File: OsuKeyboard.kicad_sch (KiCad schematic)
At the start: 31 parts, among them J1 USB_B_Micro, J2 Conn_01x04_Female, SW1 SW_Push, SW2 SW_Push, SW3 RotaryEncoder_Switch, U1 STM32F401RBTx, U2 AMS1117-3.3, Y1 16MHz

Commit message: Changed MCU and layout
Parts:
- removed C7: 100n, Capacitor_SMD:C_0402_1005Metric_Pad0.74x0.62mm_HandSolder, symbol Device:C
- removed U1: STM32F401RBTx, Package_QFP:LQFP-64_10x10mm_P0.5mm, symbol MCU_ST_STM32F4:STM32F401RBTx
- added U1: STM32F103C6Tx, Package_QFP:LQFP-48_7x7mm_P0.5mm, symbol MCU_ST_STM32F1:STM32F103C6Tx
- C10, C11: footprint Capacitor_SMD:C_0805_2012Metric_Pad1.18x1.45mm_HandSolder -> Capacitor_SMD:C_0402_1005Metric_Pad0.74x0.62mm_HandSolder
- C5, C8, C9: footprint Capacitor_SMD:C_0201_0603Metric_Pad0.64x0.40mm_HandSolder -> Capacitor_SMD:C_0402_1005Metric_Pad0.74x0.62mm_HandSolder
- R1: footprint Resistor_SMD:R_0805_2012Metric -> Resistor_SMD:R_0402_1005Metric_Pad0.72x0.64mm_HandSolder
- R2, R3, R4: footprint Resistor_SMD:R_0201_0603Metric_Pad0.64x0.40mm_HandSolder -> Resistor_SMD:R_0402_1005Metric_Pad0.72x0.64mm_HandSolder
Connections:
- net +3.3V: now also U1.1 (VBAT), U1.24 (VDD), U1.36 (VDD), U1.48 (VDD), U1.9 (VDDA)
- net GND: now also U1.23 (VSS), U1.35 (VSS), U1.47 (VSS), U1.8 (VSSA)
- net boot0: now also U1.44 (BOOT0)
- net nrst: now also U1.7 (NRST)
- net osc_in: now also U1.5 (PD0)
- net osc_out: now also U1.6 (PD1)
- net rgb1b: now also U1.18 (PB0)
- net rgb1g: now also U1.19 (PB1)
- net rgb1r: now also U1.20 (PB2)
- net rgb2b: now also U1.17 (PA7)
- net rgb2g: now also U1.16 (PA6)
- net rgb2r: now also U1.15 (PA5)
- net sw1: now also U1.22 (PB11)
- net sw2: now also U1.21 (PB10)
- net swclk: now also U1.37 (PA14)
- net swdio: now also U1.34 (PA13)
- net usb+: now also U1.33 (PA12)
- net usb-: now also U1.32 (PA11)
- net Rot_Encoder_A renamed rot_encoder_a
- net rot_encoder_a: now also U1.41 (PB5)
- net Rot_Encoder_B renamed rot_encoder_b
- net rot_encoder_b: now also U1.40 (PB4)
- net Rot_Encoder_SW renamed rot_encoder_sw
- net rot_encoder_sw: now also U1.39 (PB3)
- no-connect marks 34 -> 21
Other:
- moved on the sheet: C10, C11, C8, C9, D3, H1, H2, H3, H4, J1, J2, R4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

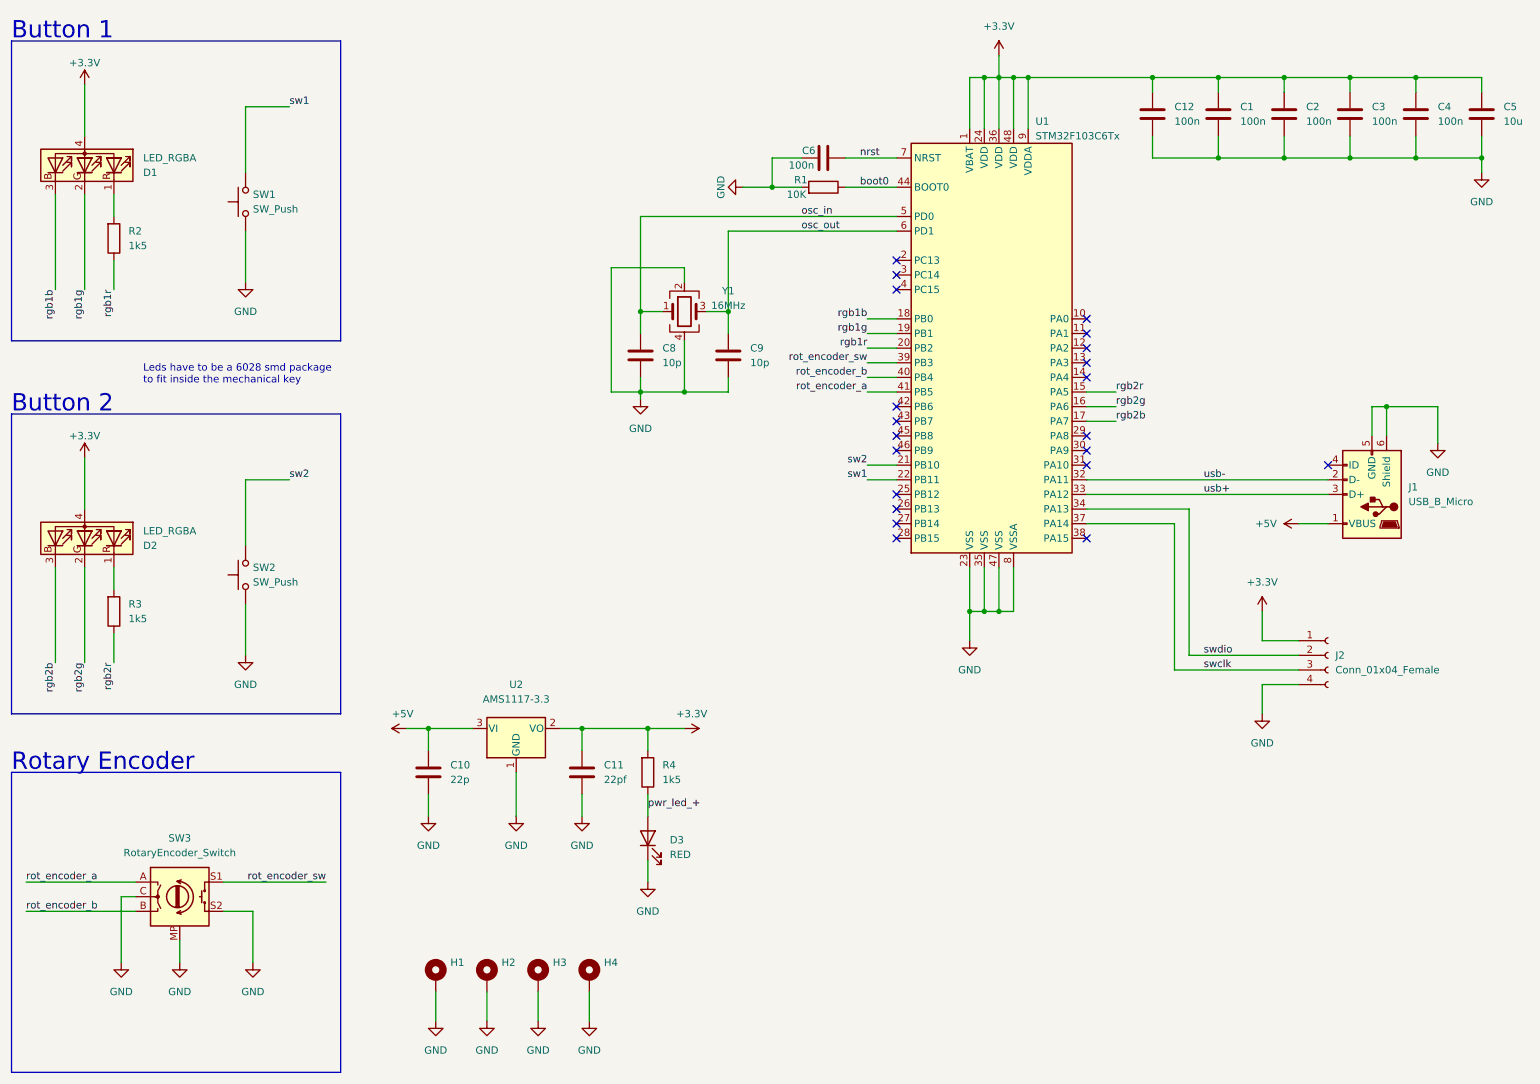
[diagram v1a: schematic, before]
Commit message: simplified and made pcb smaller
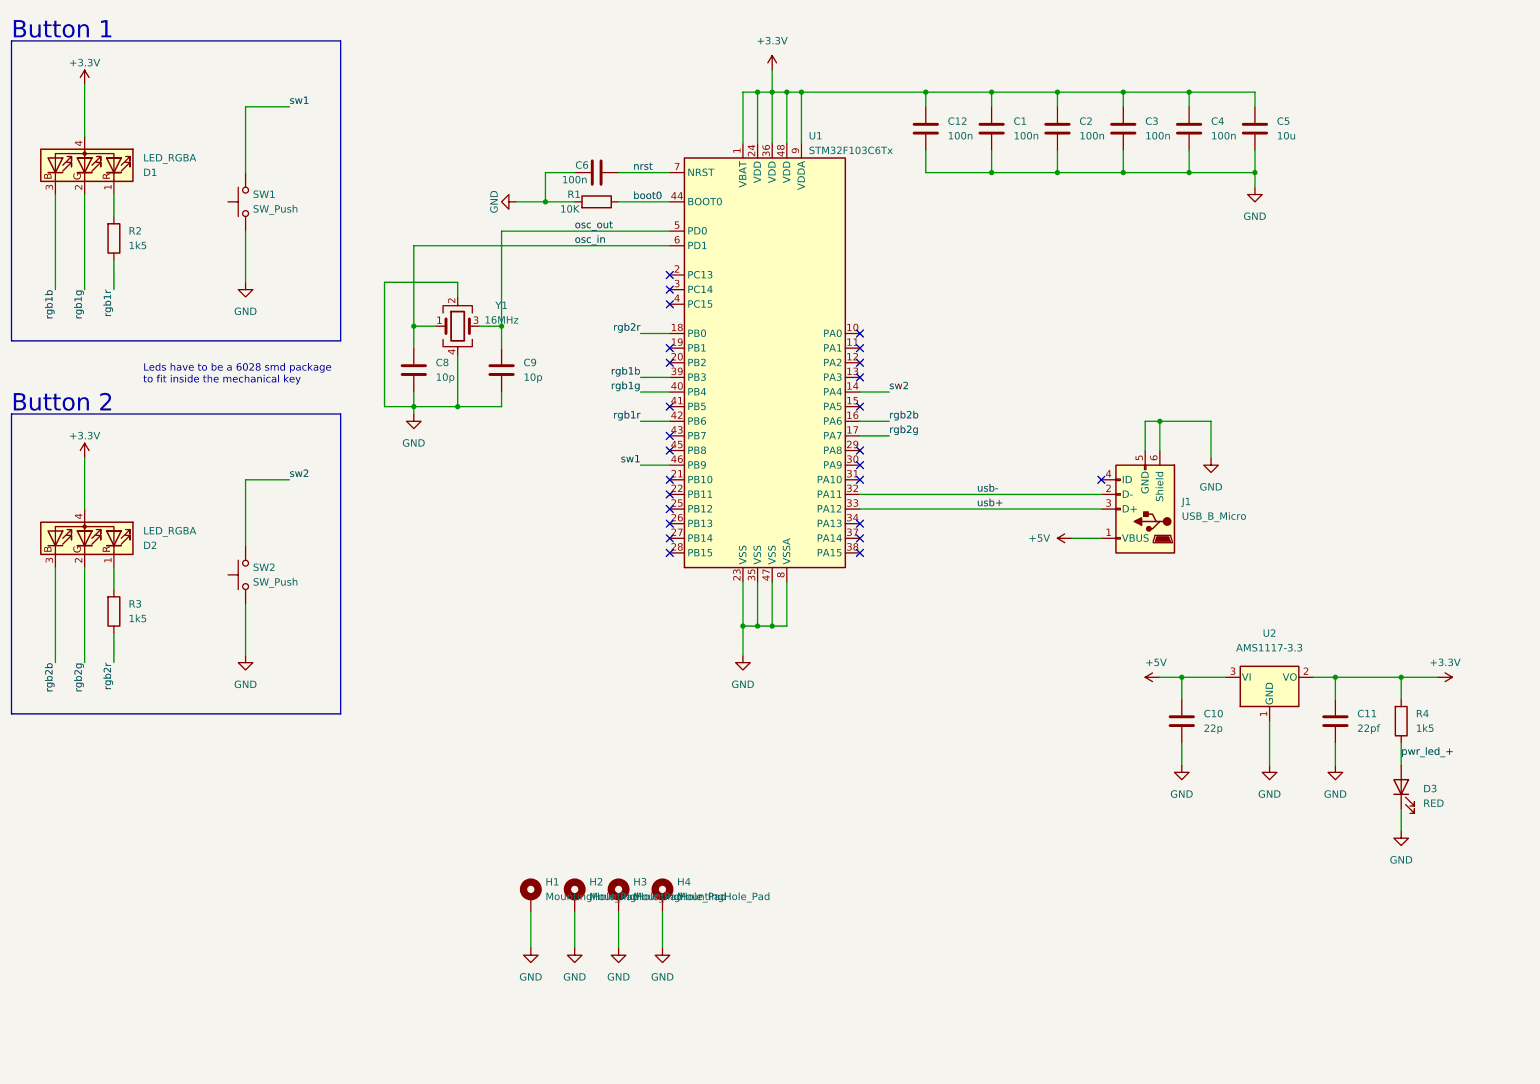
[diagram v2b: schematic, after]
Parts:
- removed J2: Conn_01x04_Female, Connector_PinHeader_2.54mm:PinHeader_1x04_P2.54mm_Vertical, symbol Connector:Conn_01x04_Female
- removed SW3: RotaryEncoder_Switch, Rotary_Encoder:RotaryEncoder_Alps_EC12E-Switch_Vertical_H20mm_CircularMountingHoles, symbol Device:RotaryEncoder_Switch
- H1, H2, H3, H4: footprint MountingHole:MountingHole_2.2mm_M2_Pad_TopBottom -> MountingHole:MountingHole_2.2mm_M2_Pad
- J1: footprint Connector_USB:USB_Micro-B_Wuerth_629105150521 -> Connector_USB:USB_Micro-B_Wuerth_629105150521_CircularHoles
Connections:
- net rot_encoder_b is gone; now on net rgb1g: U1.40 (PB4)
- net rot_encoder_sw is gone; now on net rgb1b: U1.39 (PB3)
- net osc_in: now also U1.6 (PD1); no longer U1.5 (PD0)
- net osc_out: now also U1.5 (PD0); no longer U1.6 (PD1)
- net rgb1b: no longer U1.18 (PB0)
- net rgb1g: no longer U1.19 (PB1)
- net rgb1r: now also U1.42 (PB6); no longer U1.20 (PB2)
- net rgb2b: now also U1.16 (PA6); no longer U1.17 (PA7)
- net rgb2g: now also U1.17 (PA7); no longer U1.16 (PA6)
- net rgb2r: now also U1.18 (PB0); no longer U1.15 (PA5)
- net sw1: now also U1.46 (PB9); no longer U1.22 (PB11)
- net sw2: now also U1.14 (PA4); no longer U1.21 (PB10)
- net rot_encoder_a: no longer names the net of U1.41 (PB5)
- net swclk: no longer names the net of U1.37 (PA14)
- net swdio: no longer names the net of U1.34 (PA13)
- no-connect marks 21 -> 26
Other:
- note removed: "Rotary Encoder"
- moved on the sheet: C1, C10, C11, C12, C2, C3, C4, C5, C6, C8, C9, D3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
